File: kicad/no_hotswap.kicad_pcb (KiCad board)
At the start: 2 copper layers, 143.4 x 118.2 mm, 72 parts

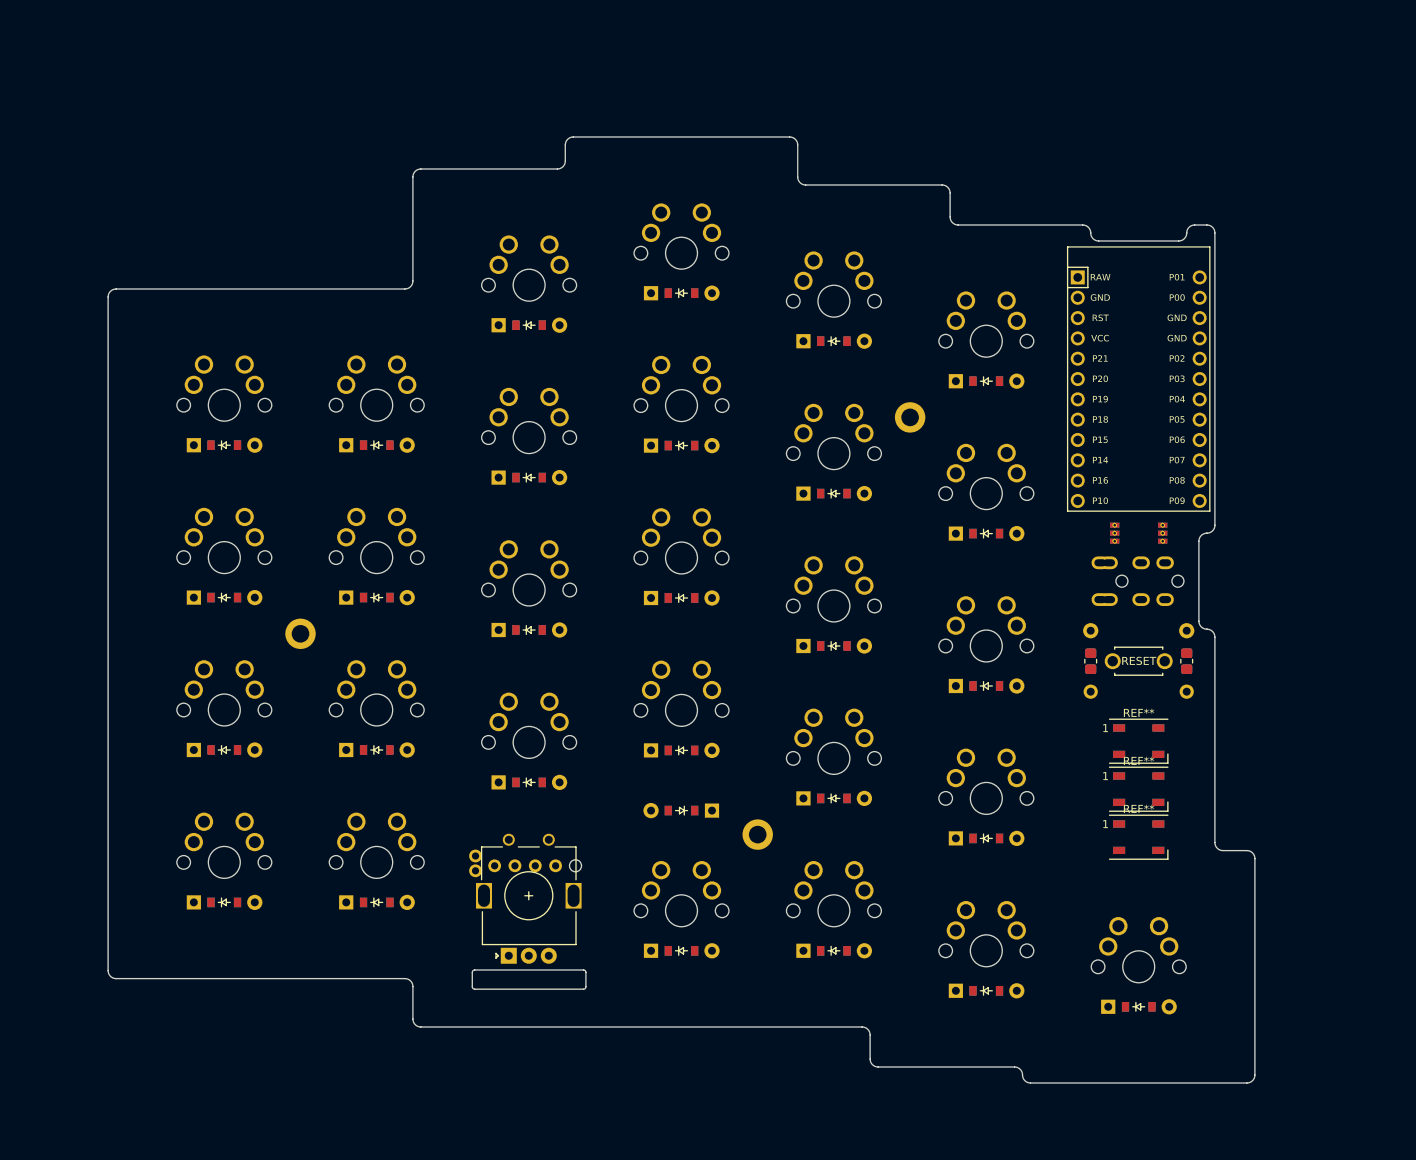
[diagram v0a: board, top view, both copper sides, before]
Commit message: change routing setup for big, beafy tracks!!
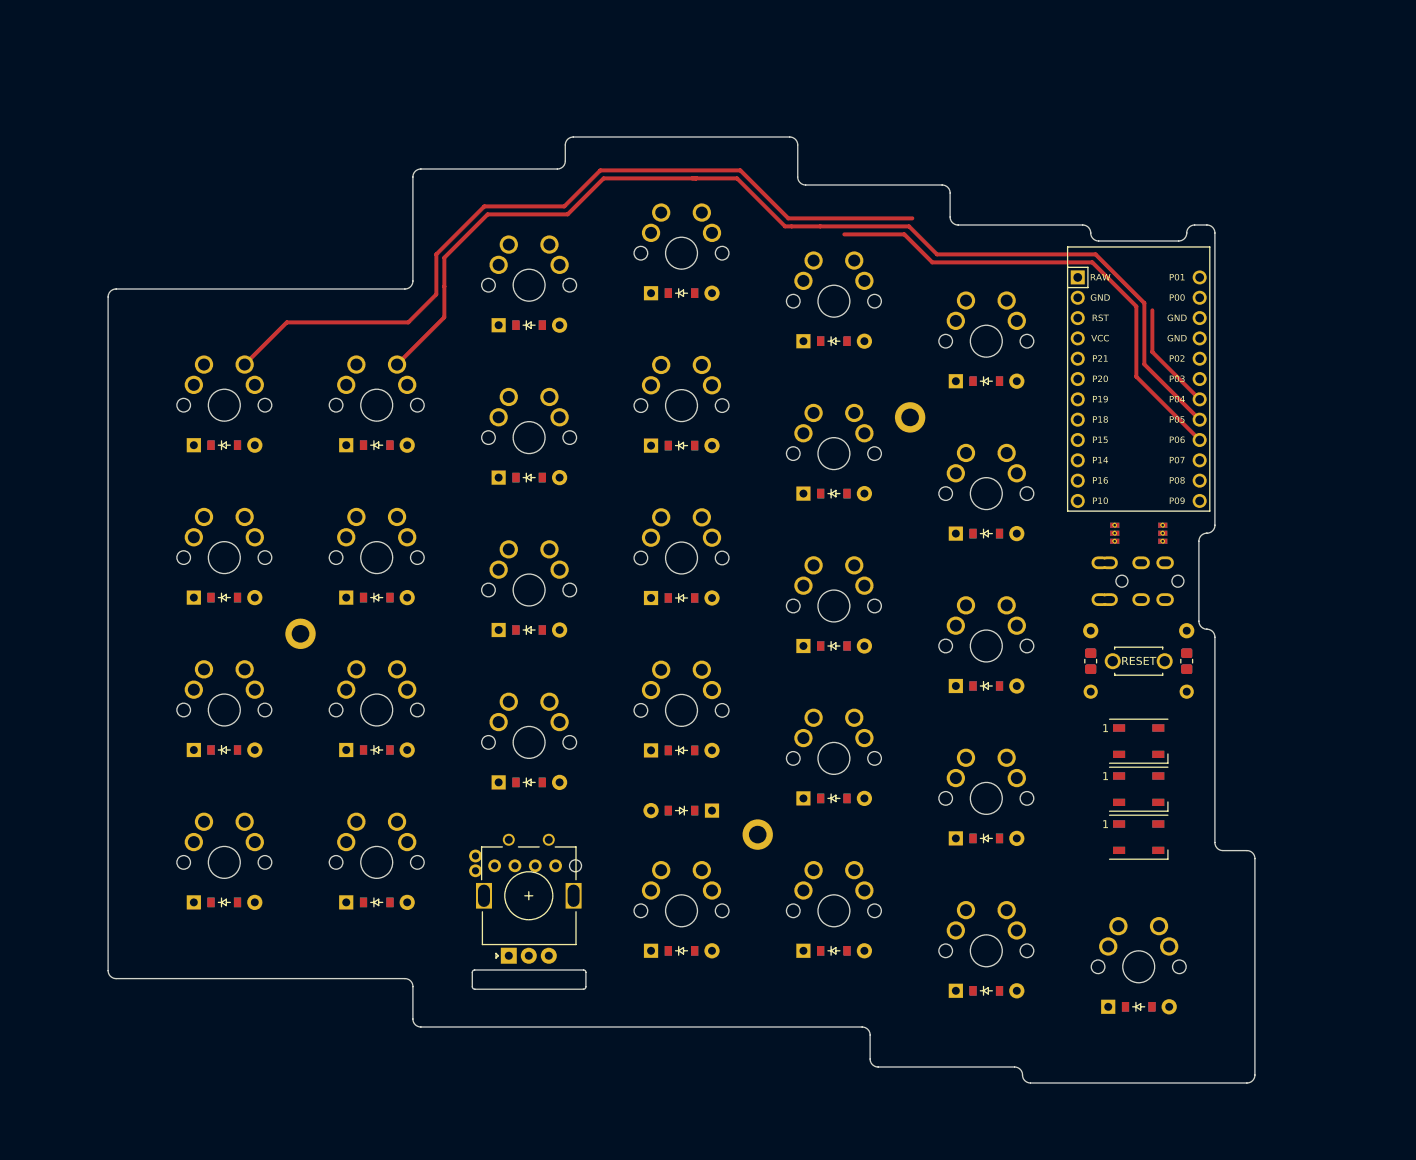
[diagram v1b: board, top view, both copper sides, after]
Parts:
- removed the REF** at (214.3, 134.9)
- removed the REF** at (214.3, 140.9)
- removed the REF** at (214.3, 146.9)
- added REF**: LED_WS2812B_PLCC4_5.0x5.0mm_P3.2mm, LED_WS2812B_PLCC4_5.0x5.0mm_P3.2mm, F.Cu at (214.3, 134.8)
- added REF**: LED_WS2812B_PLCC4_5.0x5.0mm_P3.2mm, LED_WS2812B_PLCC4_5.0x5.0mm_P3.2mm, F.Cu at (214.3, 146.8)
- added REF**: LED_WS2812B_PLCC4_5.0x5.0mm_P3.2mm, LED_WS2812B_PLCC4_5.0x5.0mm_P3.2mm, F.Cu at (214.3, 140.8)
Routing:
- net P5: track 0.00 -> 131.8 mm
- net P4: track 0.00 -> 112.5 mm
- net P6: track 0.00 -> 60.2 mm
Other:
- board size 143.4 x 118.2 mm -> 143.3 x 118.2 mm
- net class Default removed

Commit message: fix trrs jack
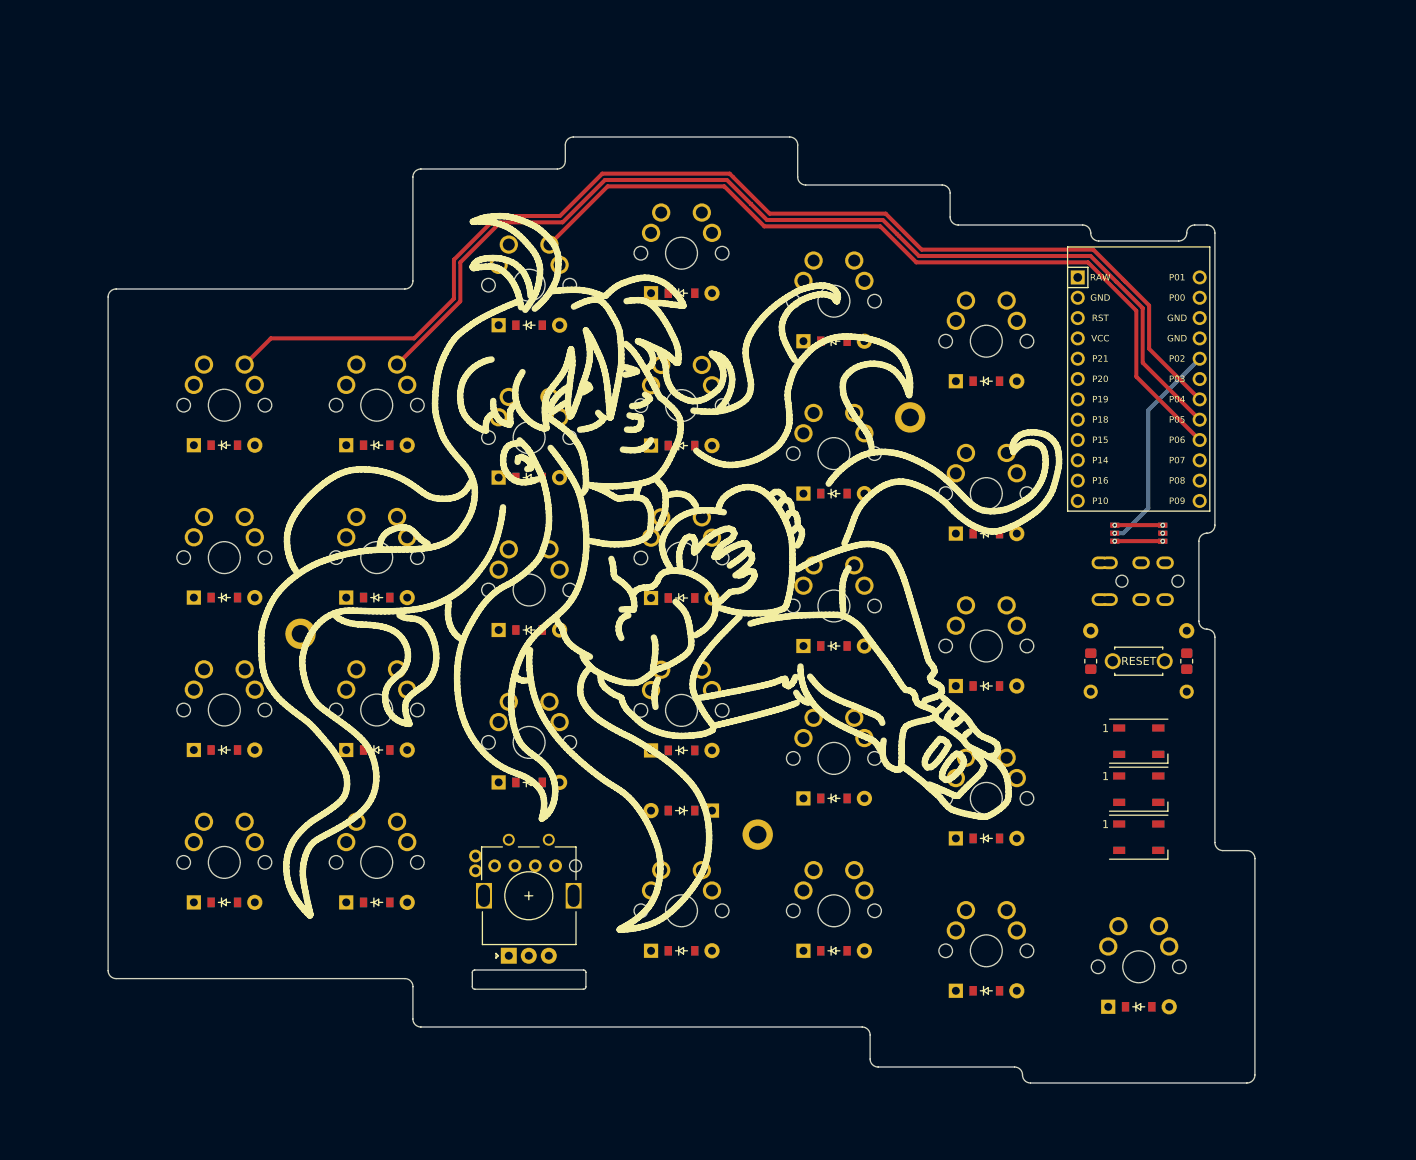
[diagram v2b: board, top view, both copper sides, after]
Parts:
- added ?: , celeste:winged-berry, B.Cu at (153.3, 113.8)
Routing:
- net P6: track 60.2 -> 102.2 mm
- net P4: track 112.5 -> 147.0 mm
- net P2: track 0.00 -> 26.8 mm, vias 0 -> 1
- net trrs_sda: track 0.00 -> 6.00 mm, vias 0 -> 2
- net trrs_gnd: track 0.00 -> 6.00 mm, vias 0 -> 2
- net P5: track 131.8 -> 129.1 mm
- net GND: vias 0 -> 1

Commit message: start routing
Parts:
- moved R1 1.00 mm to (208.3, 125.8)
- moved R2 1.00 mm to (220.3, 125.8)
- moved _1 1.00 mm to (214.3, 125.8)
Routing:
- net P21: track 0.00 -> 157.6 mm
- net P20: track 0.00 -> 137.5 mm
- net P19: track 0.00 -> 117.7 mm
- net P6: track 102.2 -> 201.2 mm
- net P4: track 147.0 -> 243.8 mm
- net P5: track 129.1 -> 224.7 mm
- net VCC: track 0.00 -> 59.8 mm
- net RST: track 0.00 -> 51.7 mm
- net P3: track 0.00 -> 45.1 mm
- net P18: track 0.00 -> 25.9 mm
- net P15: track 0.00 -> 25.9 mm
- net P14: track 0.00 -> 25.9 mm
- net ring_home: track 0.00 -> 24.5 mm
- net home_thumb: track 0.00 -> 24.5 mm
- net ring_top: track 0.00 -> 24.5 mm
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
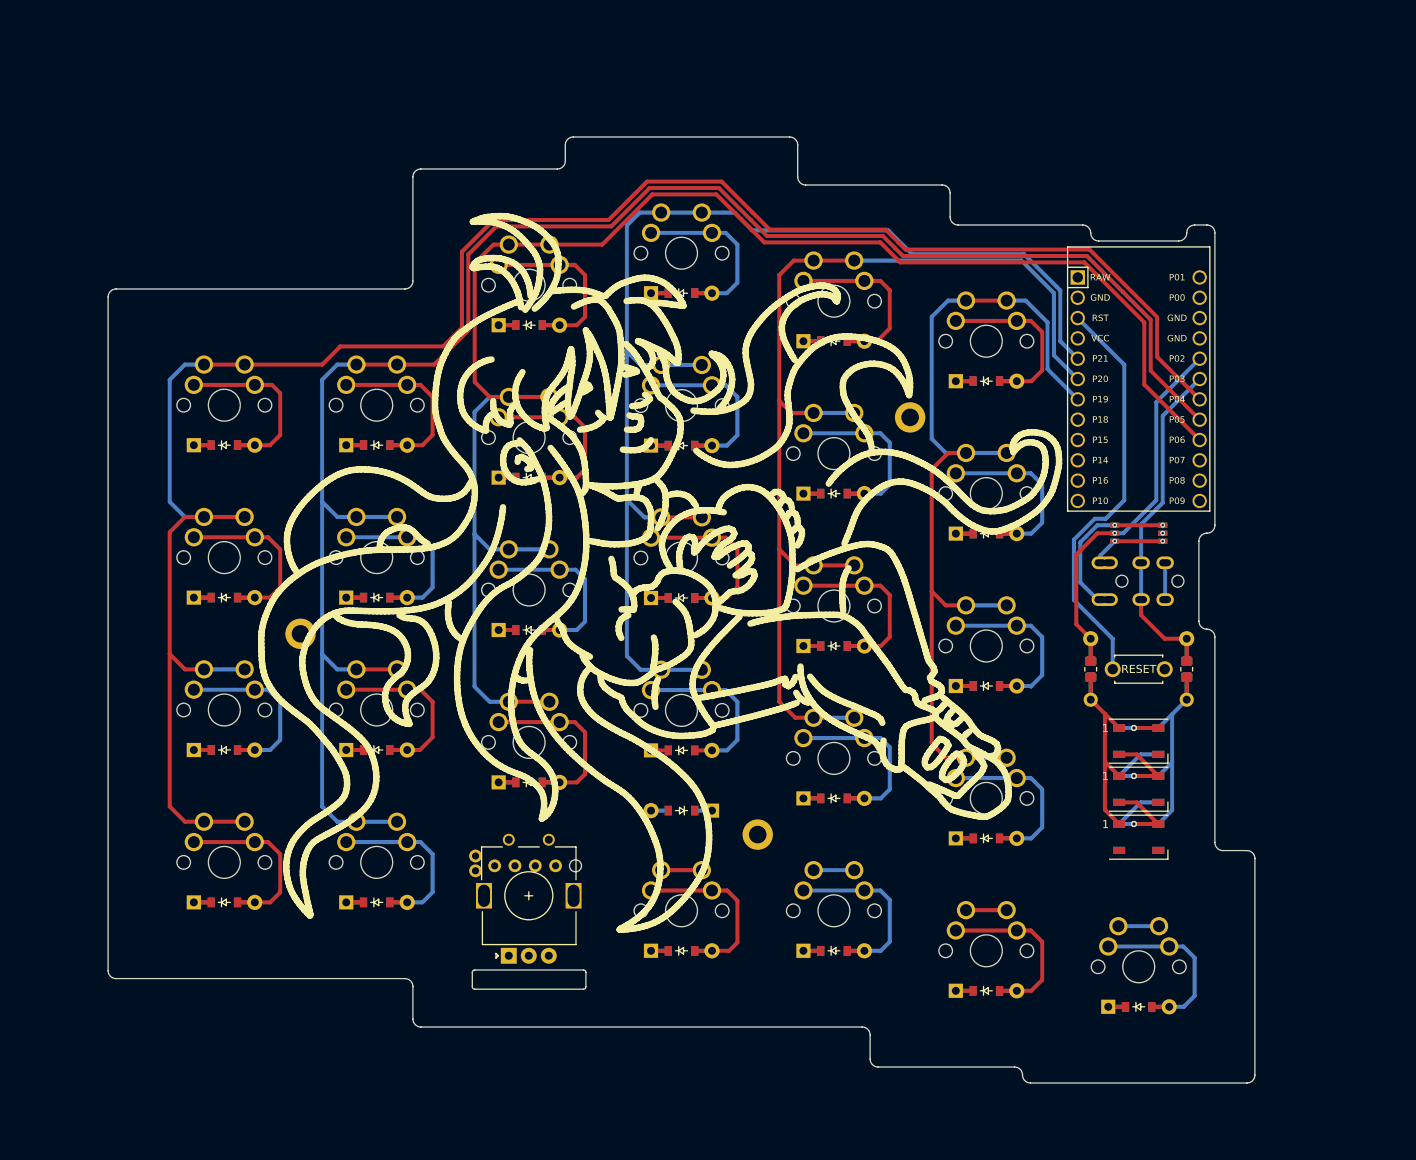
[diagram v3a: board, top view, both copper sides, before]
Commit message: routing done. silkscreen still needs attention
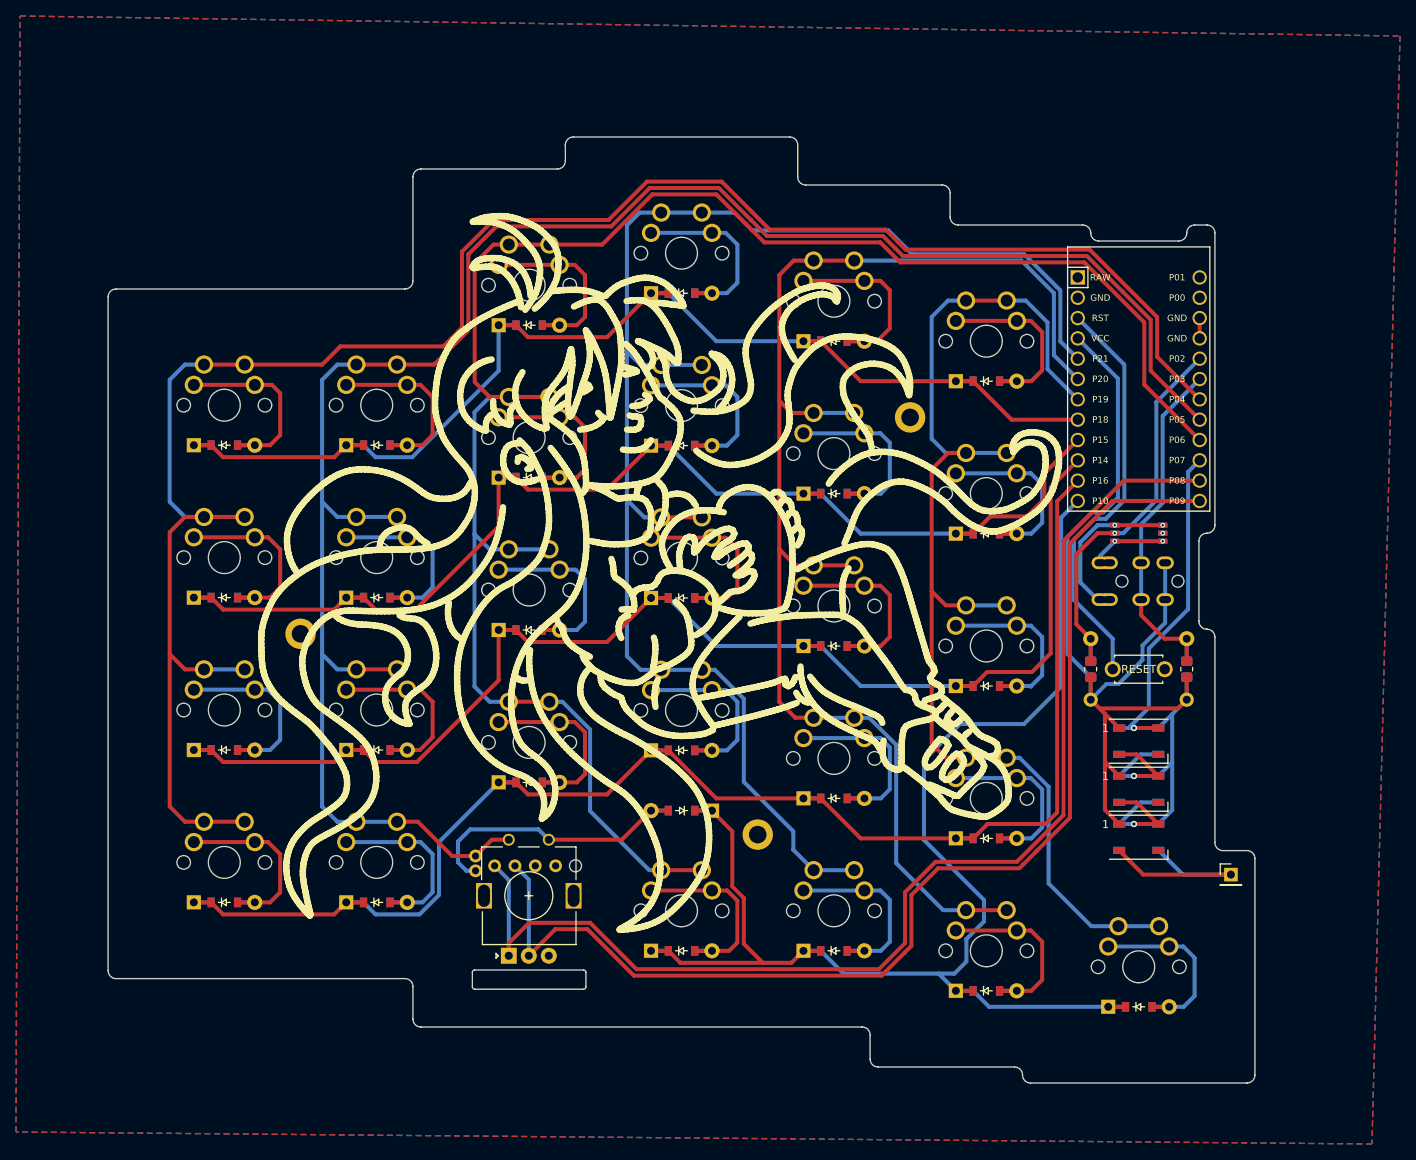
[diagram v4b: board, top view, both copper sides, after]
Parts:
- added REF**: PinHeader_1x01_P2.54mm_Vertical, Connector_PinHeader_2.54mm:PinHeader_1x01_P2.54mm_Vertical, F.Cu at (225.8, 151.5)
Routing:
- net P16: track 23.8 -> 184.8 mm
- net P10: track 19.4 -> 176.4 mm
- net P8: track 0.00 -> 152.5 mm
- net P9: track 0.00 -> 148.0 mm
- net P14: track 25.9 -> 167.1 mm
- net P15: track 25.9 -> 149.9 mm
- net P18: track 25.9 -> 144.9 mm
- net VCC: track 59.8 -> 137.4 mm
- net P7: track 4.90 -> 42.0 mm
- net my_col_row: track 2.16 -> 36.4 mm
- net P20: track 137.5 -> 170.1 mm
- net P21: track 157.6 -> 189.4 mm
- net P19: track 117.7 -> 147.4 mm
- net P6: track 201.2 -> 229.8 mm
- net rgb_3_out: track 0.00 -> 25.6 mm
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- added copper zone on B.Cu, net GND
- added copper zone on F.Cu, net GND
